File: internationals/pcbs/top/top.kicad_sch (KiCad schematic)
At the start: 26 parts, among them J1 Header-01x08, J10 JST-XH-B4B, J11 JST-XH-B6B, J12 5V-JST-XH-B2B, J13 Header-01x03, J2 5V-JST-XH-B2B, J3 Debug-JST-XH-B3B, J4 5V-JST-XH-B2B, J5 5V-JST-XH-B2B, J6 IMU-UART-JST-XH-B2B, J7 Header-01x03, J8 I2C0-JST-XH-B2B, J9 I2C1-JST-XH-B2B, M1 MotorDriver1A-XH-B4B, M2 MotorDriver1B-XH-B4B, M3 MotorDriver2A-XH-B4B, M4 MotorDriver2B-XH-B4B, P1 MotorDriver1-Power-XH-B2B, P2 MotorDriver2-Power-XH-B2B, SW1 MotorDriver-Power-SW-SPDT-XH-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, SW2 SW_Push, SW3 SW_Push, U1 Raspberry-Pi-Pico, U2 OpenMV-H7, U3 MINI560 5V

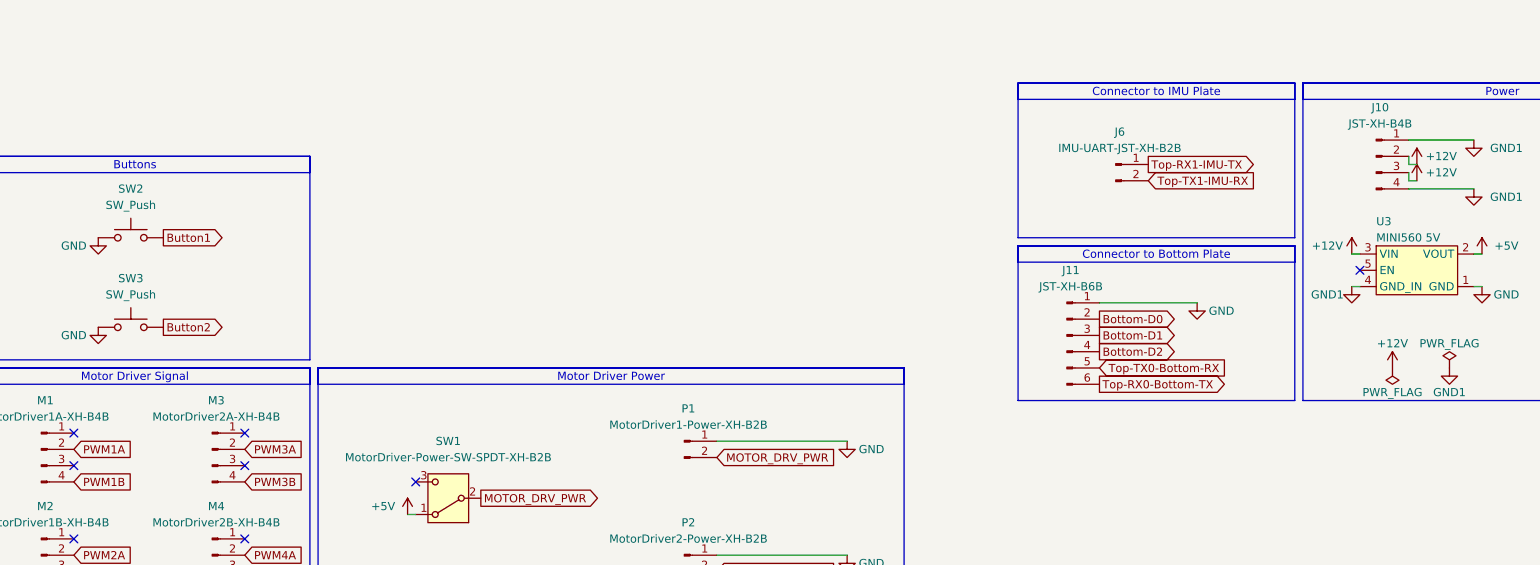
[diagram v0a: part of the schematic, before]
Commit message: pcbs: bottom: fix: use horizontal JST and update SW numbers in schematics
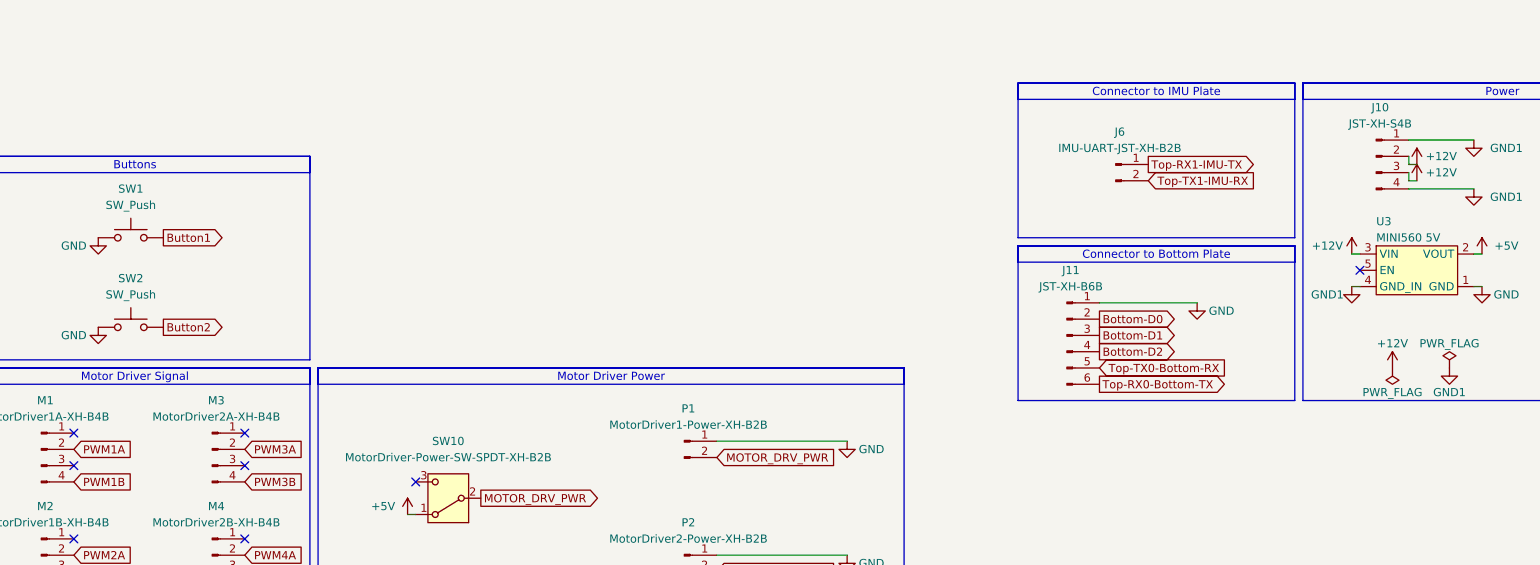
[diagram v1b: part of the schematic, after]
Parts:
- J10: value JST-XH-B4B -> JST-XH-S4B; footprint Connector_JST:JST_XH_B4B-XH-A_1x04_P2.50mm_Vertical -> Connector_JST:JST_XH_S4B-XH-A_1x04_P2.50mm_Horizontal
- renumbered SW2 to SW1, SW1 to SW10, SW3 to SW2
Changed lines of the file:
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@@
 			)
 		)
-		(property "Value" "JST-XH-B4B"
+		(property "Value" "JST-XH-S4B"
 			(at 234.315 121.92 0)
 			(effects
@@
 			)
 		)
-		(property "Footprint" "Connector_JST:JST_XH_B4B-XH-A_1x04_P2.50mm_Vertical"
+		(property "Footprint" "Connector_JST:JST_XH_S4B-XH-A_1x04_P2.50mm_Horizontal"
 			(at 233.68 127 0)
 			(effects
@@
 		(dnp no)
 		(fields_autoplaced yes)
-		(property "Reference" "SW3"
+		(property "Reference" "SW2"
 			(at 39.37 146.05 0)
 			(effects
@@
 			(project "top"
 				(path "/d681ea98-d857-49ba-b30b-b95645451bdb"
-					(reference "SW3")
+					(reference "SW2")
 					(unit 1)
 				)
@@
 		(dnp no)
 		(fields_autoplaced yes)
-		(property "Reference" "SW1"
+		(property "Reference" "SW10"
 			(at 88.9 171.45 0)
 			(effects
@@
 			(project "top"
 				(path "/d681ea98-d857-49ba-b30b-b95645451bdb"
-					(reference "SW1")
+					(reference "SW10")
 					(unit 1)
 				)
@@
 		(dnp no)
 		(fields_autoplaced yes)
-		(property "Reference" "SW2"
+		(property "Reference" "SW1"
 			(at 39.37 132.08 0)
 			(effects
@@
 			(project "top"
 				(path "/d681ea98-d857-49ba-b30b-b95645451bdb"
-					(reference "SW2")
-					(unit 1)
-				)
+					(reference "SW1")
+					(unit 1)
+				)

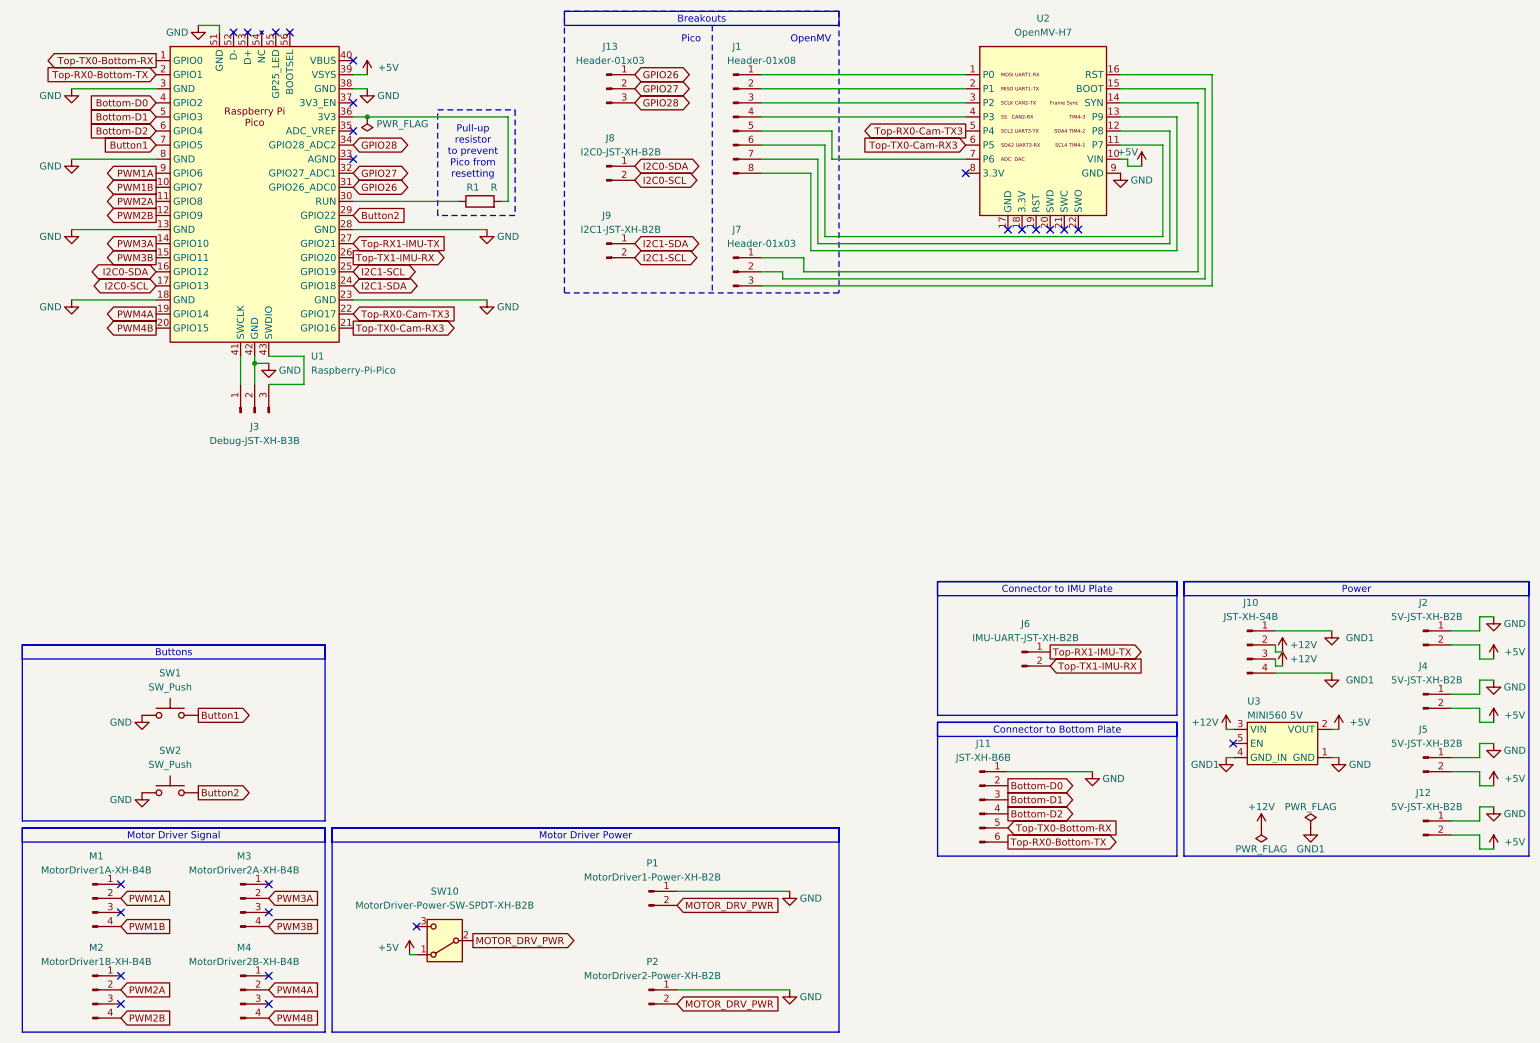
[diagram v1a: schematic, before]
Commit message: pcbs: top: feat: add mounting holes to schematics and remove GND from USB pad
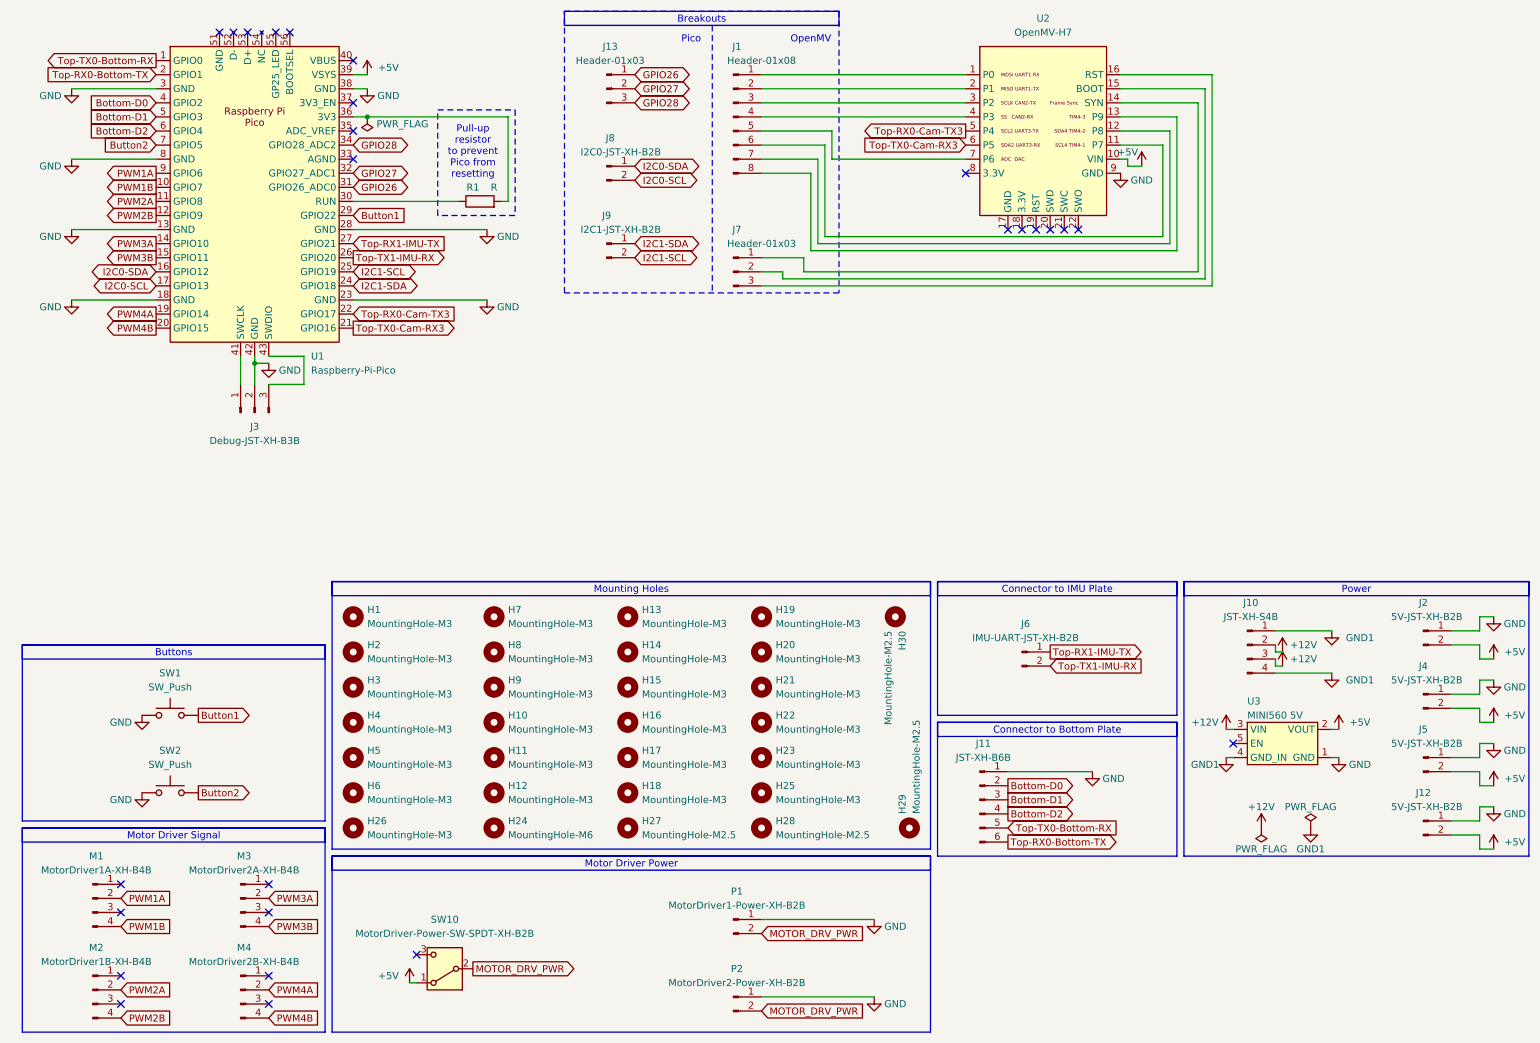
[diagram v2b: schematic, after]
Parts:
- added H1, H10, H11, H12, H13, H14, H15, H16, H17, H18, H19, H2, H20, H21, H22, H23, H25, H26, H3, H4, H5, H6, H7, H8, H9: MountingHole-M3, MountingHole:MountingHole_3.2mm_M3_Pad_Via, symbol Mechanical:MountingHole
- added H24: MountingHole-M6, MountingHole:MountingHole_6.4mm_M6_Pad_Via, symbol Mechanical:MountingHole
- added H27, H28, H29, H30: MountingHole-M2.5, MountingHole:MountingHole_2.7mm_M2.5_Pad_Via, symbol Mechanical:MountingHole
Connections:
- net Button1: now also U1.29 (GPIO22); no longer U1.7 (GPIO5)
- net Button2: now also U1.7 (GPIO5); no longer U1.29 (GPIO22)
- net GND: no longer U1.51 (GND)
- no-connect marks 25 -> 26
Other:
- moved on the sheet: P1, P2, SW10

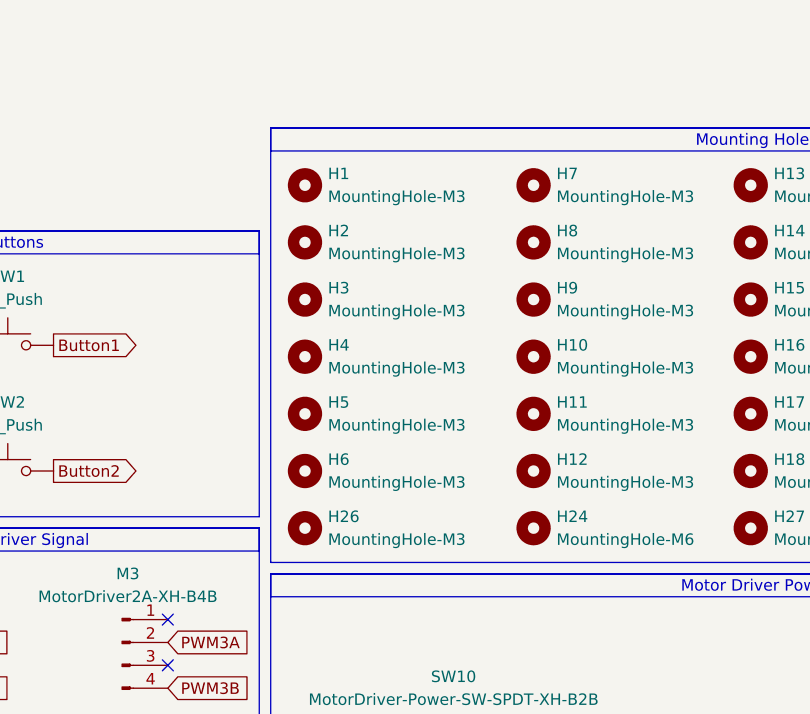
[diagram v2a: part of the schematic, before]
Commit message: pcbs: top: feat: add JLCJLCJLCJLC silkscreen
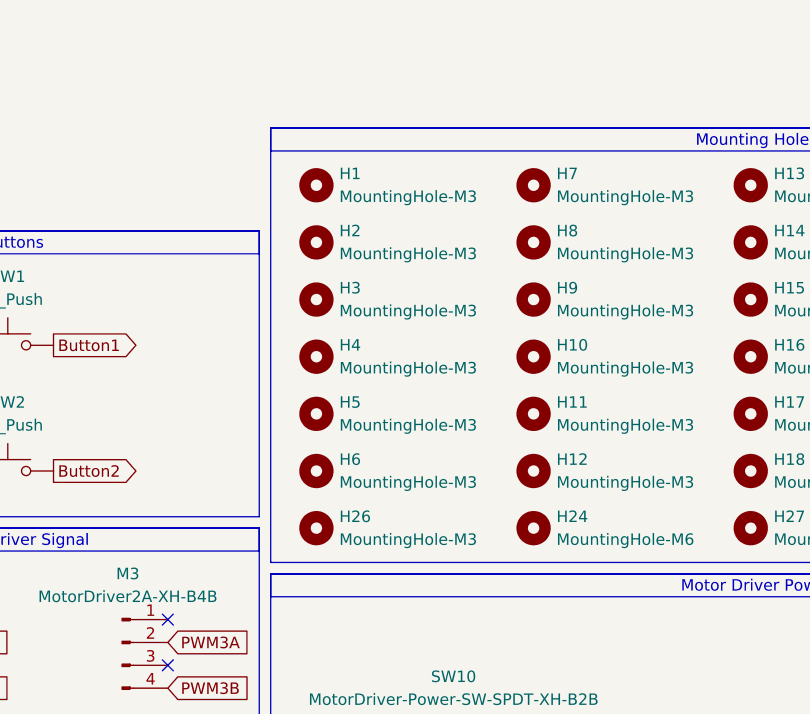
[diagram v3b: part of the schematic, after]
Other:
- moved on the sheet: H1, H2, H26, H3, H4, H5, H6
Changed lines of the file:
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@@
 	(symbol
 		(lib_id "Mechanical:MountingHole")
-		(at 72.39 147.32 0)
+		(at 73.66 147.32 0)
 		(unit 1)
 		(exclude_from_sim yes)
@@
 		(dnp no)
 		(property "Reference" "H5"
-			(at 74.93 146.0499 0)
+			(at 76.2 146.0499 0)
 			(effects
 				(font
@@
 		)
 		(property "Value" "MountingHole-M3"
-			(at 74.93 148.5899 0)
+			(at 76.2 148.5899 0)
 			(effects
 				(font
@@
 		)
 		(property "Footprint" "MountingHole:MountingHole_3.2mm_M3_Pad_Via"
-			(at 72.39 147.32 0)
+			(at 73.66 147.32 0)
 			(effects
 				(font
@@
 		)
 		(property "Datasheet" "~"
-			(at 72.39 147.32 0)
+			(at 73.66 147.32 0)
 			(effects
 				(font
@@
 		)
 		(property "Description" "Mounting Hole without connection"
-			(at 72.39 147.32 0)
+			(at 73.66 147.32 0)
 			(effects
 				(font
@@
 	(symbol
 		(lib_id "Mechanical:MountingHole")
-		(at 72.39 160.02 0)
+		(at 73.66 160.02 0)
 		(unit 1)
 		(exclude_from_sim yes)
@@
 		(dnp no)
 		(property "Reference" "H26"
-			(at 74.93 158.7499 0)
+			(at 76.2 158.7499 0)
 			(effects
 				(font
@@
 		)
 		(property "Value" "MountingHole-M3"
-			(at 74.93 161.2899 0)
+			(at 76.2 161.2899 0)
 			(effects
 				(font
@@
 		)
 		(property "Footprint" "MountingHole:MountingHole_3.2mm_M3_Pad_Via"
-			(at 72.39 160.02 0)
+			(at 73.66 160.02 0)
 			(effects
 				(font
@@
 		)
 		(property "Datasheet" "~"
-			(at 72.39 160.02 0)
+			(at 73.66 160.02 0)
 			(effects
 				(font
@@
 		)
 		(property "Description" "Mounting Hole without connection"
-			(at 72.39 160.02 0)
+			(at 73.66 160.02 0)
 			(effects
 				(font
@@
 	(symbol
 		(lib_id "Mechanical:MountingHole")
-		(at 72.39 140.97 0)
+		(at 73.66 140.97 0)
 		(unit 1)
 		(exclude_from_sim yes)
@@
 		(dnp no)
 		(property "Reference" "H4"
-			(at 74.93 139.6999 0)
+			(at 76.2 139.6999 0)
 			(effects
 				(font
@@
 		)
 		(property "Value" "MountingHole-M3"
-			(at 74.93 142.2399 0)
+			(at 76.2 142.2399 0)
 			(effects
 				(font
@@
 		)
 		(property "Footprint" "MountingHole:MountingHole_3.2mm_M3_Pad_Via"
-			(at 72.39 140.97 0)
+			(at 73.66 140.97 0)
 			(effects
 				(font
@@
 		)
 		(property "Datasheet" "~"
-			(at 72.39 140.97 0)
+			(at 73.66 140.97 0)
 			(effects
 				(font
@@
 		)
 		(property "Description" "Mounting Hole without connection"
-			(at 72.39 140.97 0)
+			(at 73.66 140.97 0)
 			(effects
 				(font
@@
 	(symbol
 		(lib_id "Mechanical:MountingHole")
-		(at 72.39 121.92 0)
+		(at 73.66 121.92 0)
 		(unit 1)
 		(exclude_from_sim yes)
@@
 		(dnp no)
 		(property "Reference" "H1"
-			(at 74.93 120.6499 0)
+			(at 76.2 120.6499 0)
 			(effects
 				(font
@@
 		)
 		(property "Value" "MountingHole-M3"
-			(at 74.93 123.1899 0)
+			(at 76.2 123.1899 0)
 			(effects
 				(font
@@
 		)
 		(property "Footprint" "MountingHole:MountingHole_3.2mm_M3_Pad_Via"
-			(at 72.39 121.92 0)
+			(at 73.66 121.92 0)
 			(effects
 				(font
@@
 		)
 		(property "Datasheet" "~"
-			(at 72.39 121.92 0)
+			(at 73.66 121.92 0)
 			(effects
 				(font
@@
 		)
 		(property "Description" "Mounting Hole without connection"
-			(at 72.39 121.92 0)
+			(at 73.66 121.92 0)
 			(effects
 				(font
@@
 	(symbol
 		(lib_id "Mechanical:MountingHole")
-		(at 72.39 128.27 0)
+		(at 73.66 128.27 0)
 		(unit 1)
 		(exclude_from_sim yes)
@@
 		(dnp no)
 		(property "Reference" "H2"
-			(at 74.93 126.9999 0)
+			(at 76.2 126.9999 0)
 			(effects
 				(font
@@
 		)
 		(property "Value" "MountingHole-M3"
-			(at 74.93 129.5399 0)
+			(at 76.2 129.5399 0)
 			(effects
 				(font
@@
 		)
 		(property "Footprint" "MountingHole:MountingHole_3.2mm_M3_Pad_Via"
-			(at 72.39 128.27 0)
+			(at 73.66 128.27 0)
 			(effects
 				(font
@@
 		)
 		(property "Datasheet" "~"
-			(at 72.39 128.27 0)
+			(at 73.66 128.27 0)
 			(effects
 				(font
@@
 		)
 		(property "Description" "Mounting Hole without connection"
-			(at 72.39 128.27 0)
+			(at 73.66 128.27 0)
 			(effects
 				(font
@@
 	(symbol
 		(lib_id "Mechanical:MountingHole")
-		(at 72.39 153.67 0)
+		(at 73.66 153.67 0)
 		(unit 1)
 		(exclude_from_sim yes)
@@
 		(fields_autoplaced yes)
 		(property "Reference" "H6"
-			(at 74.93 152.3999 0)
+			(at 76.2 152.3999 0)
 			(effects
 				(font
@@
 		)
 		(property "Value" "MountingHole-M3"
-			(at 74.93 154.9399 0)
+			(at 76.2 154.9399 0)
 			(effects
 				(font
@@
 		)
 		(property "Footprint" "MountingHole:MountingHole_3.2mm_M3_Pad_Via"
-			(at 72.39 153.67 0)
+			(at 73.66 153.67 0)
 			(effects
 				(font
@@
 		)
 		(property "Datasheet" "~"
-			(at 72.39 153.67 0)
+			(at 73.66 153.67 0)
 			(effects
 				(font
@@
 		)
 		(property "Description" "Mounting Hole without connection"
-			(at 72.39 153.67 0)
+			(at 73.66 153.67 0)
 			(effects
 				(font
@@
 	(symbol
 		(lib_id "Mechanical:MountingHole")
-		(at 72.39 134.62 0)
+		(at 73.66 134.62 0)
 		(unit 1)
 		(exclude_from_sim yes)
@@
 		(dnp no)
 		(property "Reference" "H3"
-			(at 74.93 133.3499 0)
+			(at 76.2 133.3499 0)
 			(effects
 				(font
@@
 		)
 		(property "Value" "MountingHole-M3"
-			(at 74.93 135.8899 0)
+			(at 76.2 135.8899 0)
 			(effects
 				(font
@@
 		)
 		(property "Footprint" "MountingHole:MountingHole_3.2mm_M3_Pad_Via"
-			(at 72.39 134.62 0)
+			(at 73.66 134.62 0)
 			(effects
 				(font
@@
 		)
 		(property "Datasheet" "~"
-			(at 72.39 134.62 0)
+			(at 73.66 134.62 0)
 			(effects
 				(font
@@
 		)
 		(property "Description" "Mounting Hole without connection"
-			(at 72.39 134.62 0)
+			(at 73.66 134.62 0)
 			(effects
 				(font
